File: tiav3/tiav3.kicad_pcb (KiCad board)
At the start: 4 copper layers, 25.3 x 25.3 mm, 21 parts, among them J1 SSQ-103-01-G-D, J2 Conn_Coaxial, U1 OPA847IDBVT

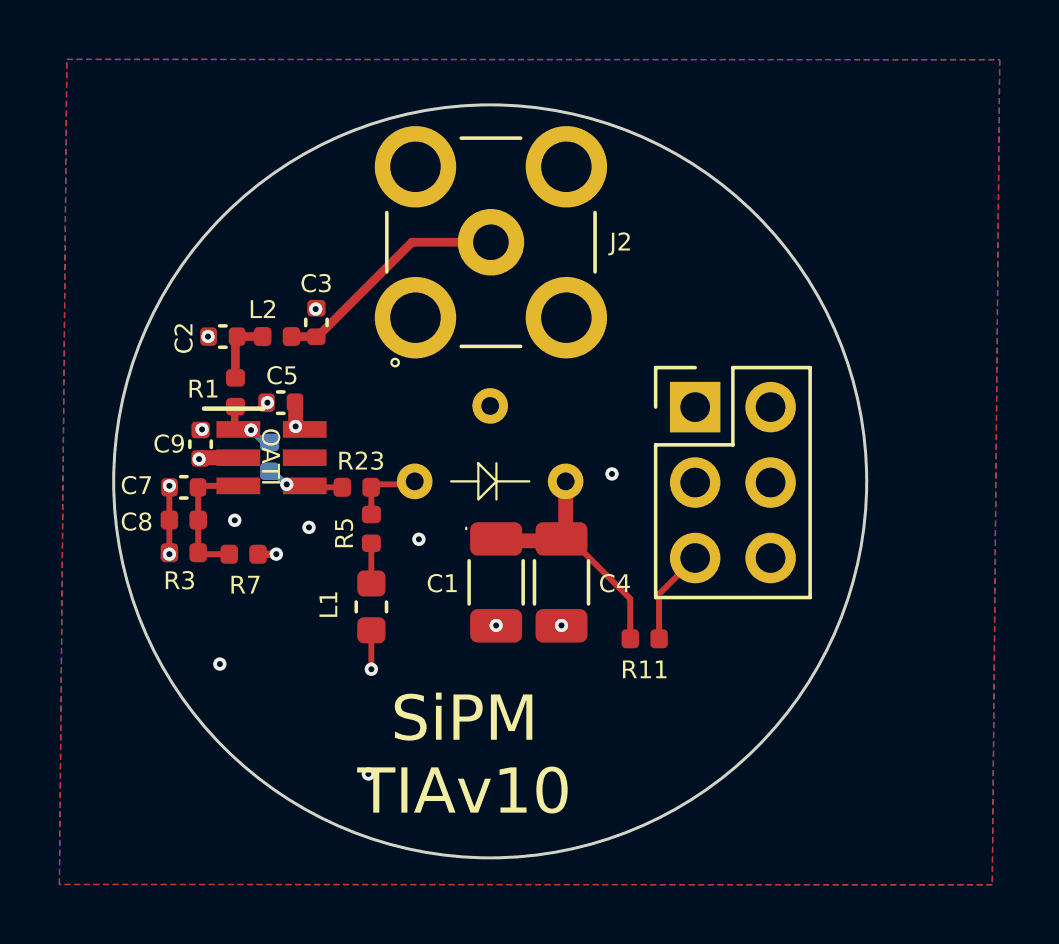
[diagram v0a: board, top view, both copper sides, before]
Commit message: Improve low pass filter documentation and change default cut off
The 27 MHz default was a bit high since most objectives would not need this when paired with a 16 or 24 KHz scanner.

Adjust some of the footprints and text.

Bump to V11 to reflect the changed default LPF values.
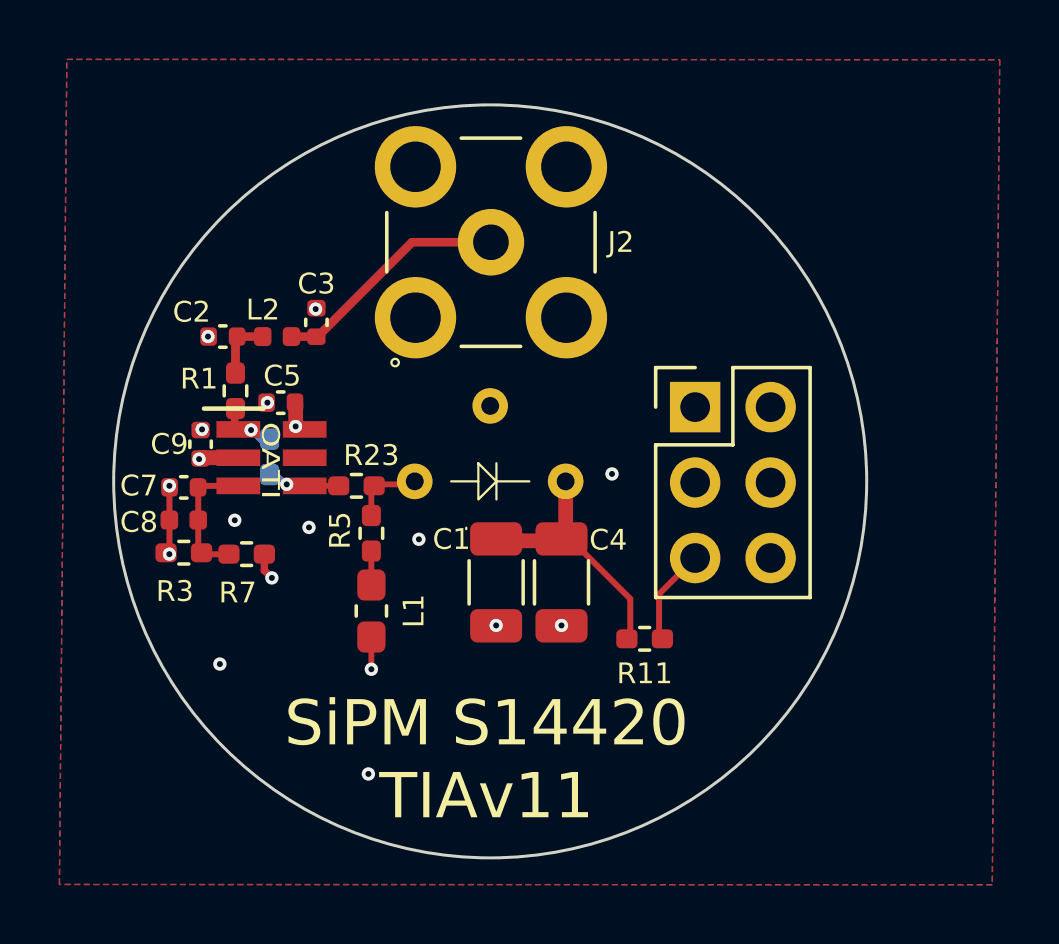
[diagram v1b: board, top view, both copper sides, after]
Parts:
- C2: value 120pF -> 330pF
- C3: value 120p -> 330p
- C7: value 0.1u -> 1u
- L1: footprint footprints:L_0603_1608Metric -> Inductor_SMD:L_0603_1608Metric_Pad1.05x0.95mm_HandSolder
- L2: value 560nH -> 1500nH
- R1, R11, R2, R23, R3, R5, R7: footprint footprints:R_0402_1005Metric -> Resistor_SMD:R_0402_1005Metric_Pad0.72x0.64mm_HandSolder
- moved R5 0.15 mm to (196.0, 101.7)
- moved L1 0.14 mm to (196.0, 104.4)
- moved R7 0.10 mm to (191.8, 102.5)
- moved R23 0.05 mm to (195.5, 100.2)
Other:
- board text added: "SiPM S14420 TIAv11"
- board text removed: "SiPM TIAv10"

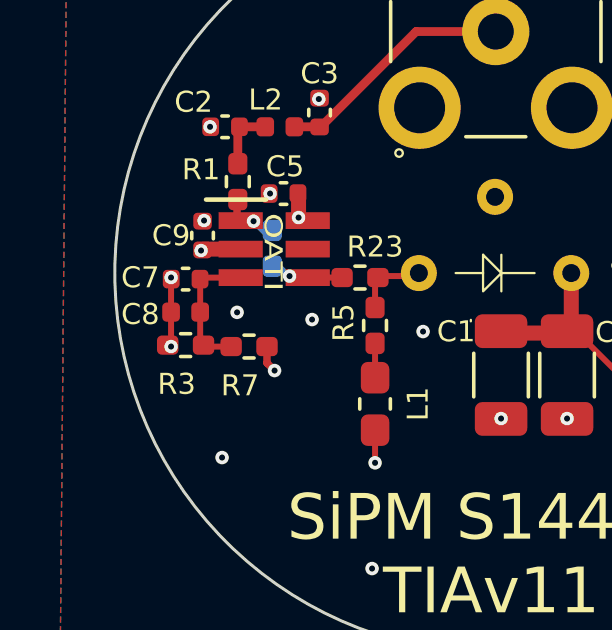
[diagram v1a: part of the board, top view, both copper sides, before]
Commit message: Delete unneeded footprints
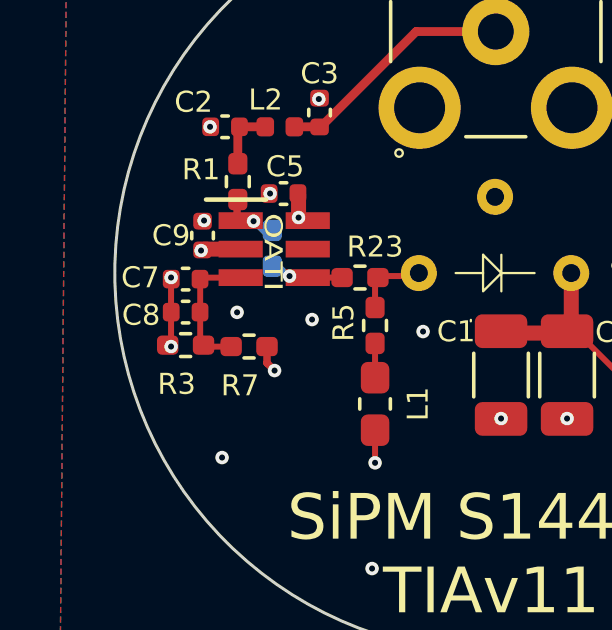
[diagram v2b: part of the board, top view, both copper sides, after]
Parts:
- C8: footprint footprints:C_0402_1005Metric -> Capacitor_SMD:C_0402_1005Metric
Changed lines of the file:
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@@
 			(psa4output no)
 			(plot_black_and_white yes)
-			(plotinvisibletext no)
 			(sketchpadsonfab no)
 			(plotpadnumbers no)
@@
 			)
 		)
-		(property "Datasheet" ""
+		(property "Datasheet" "~"
 			(at 0 0 270)
 			(layer "F.Fab")
@@
 			)
 		)
-		(property "Datasheet" ""
+		(property "Datasheet" "~"
 			(at 0 0 180)
 			(layer "F.Fab")
@@
 			)
 		)
-		(property "Datasheet" ""
+		(property "Datasheet" "~"
 			(at 0 0 180)
 			(layer "F.Fab")
@@
 		)
 	)
-	(footprint "footprints:C_0402_1005Metric"
+	(footprint "Capacitor_SMD:C_0402_1005Metric"
 		(layer "F.Cu")
 		(at 189.6854 101.3018 180)
-		(descr "Capacitor SMD 0402 (1005 Metric), square (rectangular) end terminal, IPC_7351 nominal, (Body size source: http://www.tortai-tech.com/upload/download/2011102023233369053.pdf), generated with kicad-footprint-generator")
+		(descr "Capacitor SMD 0402 (1005 Metric), square (rectangular) end terminal, IPC-7351 nominal, (Body size source: IPC-SM-782 page 76, https://www.pcb-3d.com/wordpress/wp-content/uploads/ipc-sm-782a_amendment_1_and_2.pdf), generated with kicad-footprint-generator")
 		(tags "capacitor")
 		(property "Reference" "C8"
-			(at 1.5104 -0.0732 0)
+			(at 1.4854 -0.0982 180)
 			(layer "F.SilkS")
 			(effects
@@
 		)
 		(property "Value" "1u"
-			(at 0 1.17 0)
+			(at 0 1.16 180)
 			(layer "F.Fab")
-			(hide yes)
 			(effects
 				(font
@@
 			)
 		)
-		(property "Datasheet" ""
+		(property "Datasheet" "~"
 			(at 0 0 180)
 			(layer "F.Fab")
@@
 		(attr smd)
 		(fp_line
-			(start 0.93 0.47)
-			(end -0.93 0.47)
+			(start -0.107836 0.36)
+			(end 0.107836 0.36)
+			(stroke
+				(width 0.12)
+				(type solid)
+			)
+			(layer "F.SilkS")
+		)
+		(fp_line
+			(start -0.107836 -0.36)
+			(end 0.107836 -0.36)
+			(stroke
+				(width 0.12)
+				(type solid)
+			)
+			(layer "F.SilkS")
+		)
+		(fp_line
+			(start 0.91 0.46)
+			(end -0.91 0.46)
 			(stroke
 				(width 0.05)
@@
 		)
 		(fp_line
-			(start 0.93 -0.47)
-			(end 0.93 0.47)
+			(start 0.91 -0.46)
+			(end 0.91 0.46)
 			(stroke
 				(width 0.05)
@@
 		)
 		(fp_line
-			(start -0.93 0.47)
-			(end -0.93 -0.47)
+			(start -0.91 0.46)
+			(end -0.91 -0.46)
 			(stroke
 				(width 0.05)
@@
 		)
 		(fp_line
-			(start -0.93 -0.47)
-			(end 0.93 -0.47)
+			(start -0.91 -0.46)
+			(end 0.91 -0.46)
 			(stroke
 				(width 0.05)
@@
 		)
 		(fp_text user "${REFERENCE}"
-			(at 0 0 0)
+			(at 0 0 180)
 			(layer "F.Fab")
 			(effects
@@
 		)
 		(pad "1" smd roundrect
-			(at -0.485 0 180)
-			(size 0.59 0.64)
+			(at -0.48 0 180)
+			(size 0.56 0.62)
 			(layers "F.Cu" "F.Mask" "F.Paste")
 			(roundrect_rratio 0.25)
@@
 		)
 		(pad "2" smd roundrect
-			(at 0.485 0 180)
-			(size 0.59 0.64)
+			(at 0.48 0 180)
+			(size 0.56 0.62)
 			(layers "F.Cu" "F.Mask" "F.Paste")
 			(roundrect_rratio 0.25)
@@
 		)
 		(embedded_fonts no)
-		(model "${KISYS3DMOD}/Capacitor_SMD.3dshapes/C_0402_1005Metric.wrl"
+		(model "${KICAD9_3DMODEL_DIR}/Capacitor_SMD.3dshapes/C_0402_1005Metric.step"
 			(offset
 				(xyz 0 0 0)
@@
 			)
 		)
-		(property "Datasheet" ""
+		(property "Datasheet" "~"
 			(at 0 0 0)
 			(unlocked yes)
@@
 			)
 		)
-		(property "Datasheet" ""
+		(property "Datasheet" "~"
 			(at 0 0 180)
 			(unlocked yes)
@@
 			(layer "F.Fab")
 		)
-		(fp_text user "${REFERENCE}"
-			(at 1.27 2.54 90)
-			(layer "F.Fab")
-			(hide yes)
-			(effects
-				(font
-					(size 1 1)
-					(thickness 0.15)
-				)
-			)
-		)
 		(pad "1" thru_hole rect
 			(at 0 0)
@@
 			)
 		)
-		(property "Datasheet" ""
+		(property "Datasheet" "~"
 			(at 0 0 180)
 			(unlocked yes)
@@
 			)
 		)
-		(property "Datasheet" ""
+		(property "Datasheet" "~"
 			(at 0 0 90)
 			(unlocked yes)
@@
 			)
 		)
-		(property "Datasheet" ""
+		(property "Datasheet" "~"
 			(at 0 0 90)
 			(layer "F.Fab")
@@
 			)
 		)
-		(property "Datasheet" ""
+		(property "Datasheet" "~"
 			(at 0 0 90)
 			(unlocked yes)
@@
 			)
 		)
-		(property "Datasheet" ""
+		(property "Datasheet" "~"
 			(at 0 0 0)
 			(unlocked yes)
@@
 			)
 		)
-		(property "Datasheet" ""
+		(property "Datasheet" "~"
 			(at 0 0 90)
 			(layer "F.Fab")
@@
 			)
 		)
-		(property "Datasheet" ""
+		(property "Datasheet" "~"
 			(at 0 0 180)
 			(layer "F.Fab")
@@
 			)
 		)
-		(property "Datasheet" ""
+		(property "Datasheet" "~"
 			(at 0 0 270)
 			(layer "F.Fab")
@@
 			)
 		)
-		(property "Datasheet" ""
+		(property "Datasheet" "~"
 			(at 0 0 270)
 			(unlocked yes)
